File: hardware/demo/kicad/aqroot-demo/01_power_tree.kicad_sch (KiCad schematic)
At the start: 138 parts, among them J3 USB_C_Receptacle_USB2.0_16P, J4 BATTERY PIGTAIL 26AWG, Q2 NTMD4820N, Q3 NTMD4820N, Q4 BSS138, Q5 AO3401A, Q6 BSS138, Q7 BSS138, Q8 BSS138, Q9 BSS138, SW9 SW_SPDT, U10 USBLC6-2SC6, U11 BQ25185, U12 TPS63020, U13 TPS61023, U14 MAX17048, U18 LTC4368-1, U19 TLV7032, U20 TPS22950-Q1, U21 TPS61023, U22 TPS22950-Q1

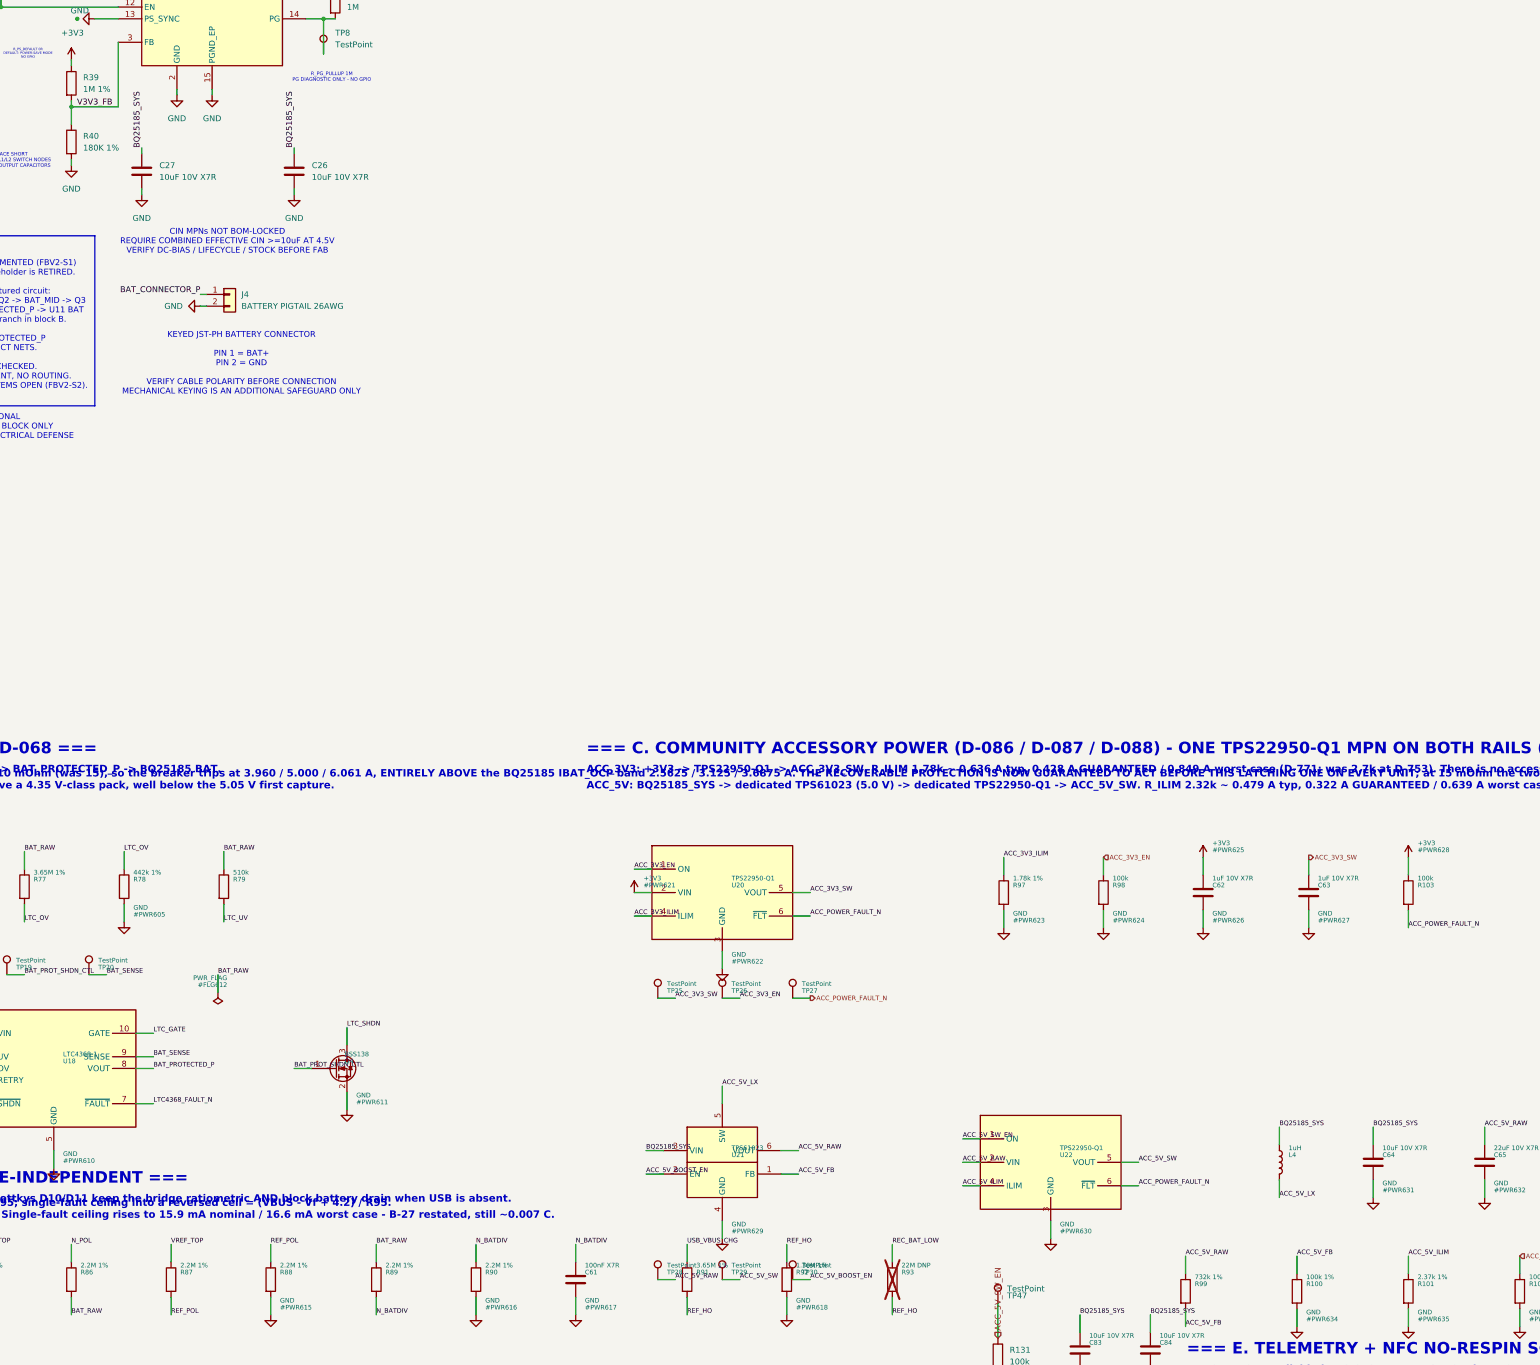
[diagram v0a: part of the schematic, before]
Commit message: demo: D-787 close Round-6 accessory-voltage contract and release proofs
R6-A01. The accessory proof costed +3V3 as an ideal 3.3 V source, so the
Community Port's published 3.135 V minimum was not guaranteed at the published
400 mA. F6 now derives the TPS63020 rail from the fitted divider, its value
tolerance, the SELECTED PART's TCR keyed to the purchased MPN, TI SLVS916I's
495/500/505 mV feedback band, 0.5% line and 0.5% load regulation, and the +5%
power-save high side.

R39 = 1 MOhm 0.1% / 25 ppm (Viking ARG03BTC1004) and R40 = 178 kOhm 0.1% /
25 ppm (Viking ARG03BTC1783). 176 kOhm was the first candidate and is refused
on AVAILABILITY: every 176 kOhm 0603 part at 0.1% or better in the JLCPCB
catalogue reads stock 0, including the KOA RN73H1JTTD1763B10 the first draft
locked, so it fails this repository's own rule_open_sourcing liquidity floor.
F7 now carries that as a clause -- every locked part must have an archived
exact-MPN live record clearing five boards x 10 -- with the zero-stock part and
a no-record part as refused controls.

Derived envelope: raw PWM 3.261337 / 3.308989 / 3.357013 V, heavy-load minimum
3.228806 V, power-save high 3.542487 V against the 3.600 V internal ceiling,
and 3.146366 V delivered at either J5 3.3 V contact at 400 mA against the
3.135 V contract, over the bounded U20->TP12 copper, the <=30 mOhm manual
first-five reinforcement lead and U20's 68 mOhm maximum RON. F6 proves off the
live netlist that TP12.1, J5.3 and J5.22 are all on /ACC_3V3_SW.

R101 = 2.43 kOhm guarantees 0.3065 A on ACC_5V and leaves the worst
user-reachable limiter state 1.49% below IBAT_OCP minimum. The dual loaded-VCELL
requirement re-derives to 3.8094 V -> 3.85 V firmware floor; single-rail is
3.1671 V so the 3.50 V policy stands.

R6-E01/E02. Both safety sequences move into a compiled host-tested seam and six
evasions are caught. New H8 proves the SHIPPED firmware calls that seam and
keeps no untested copy beside it. F5's three backlight controls, which an
ear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
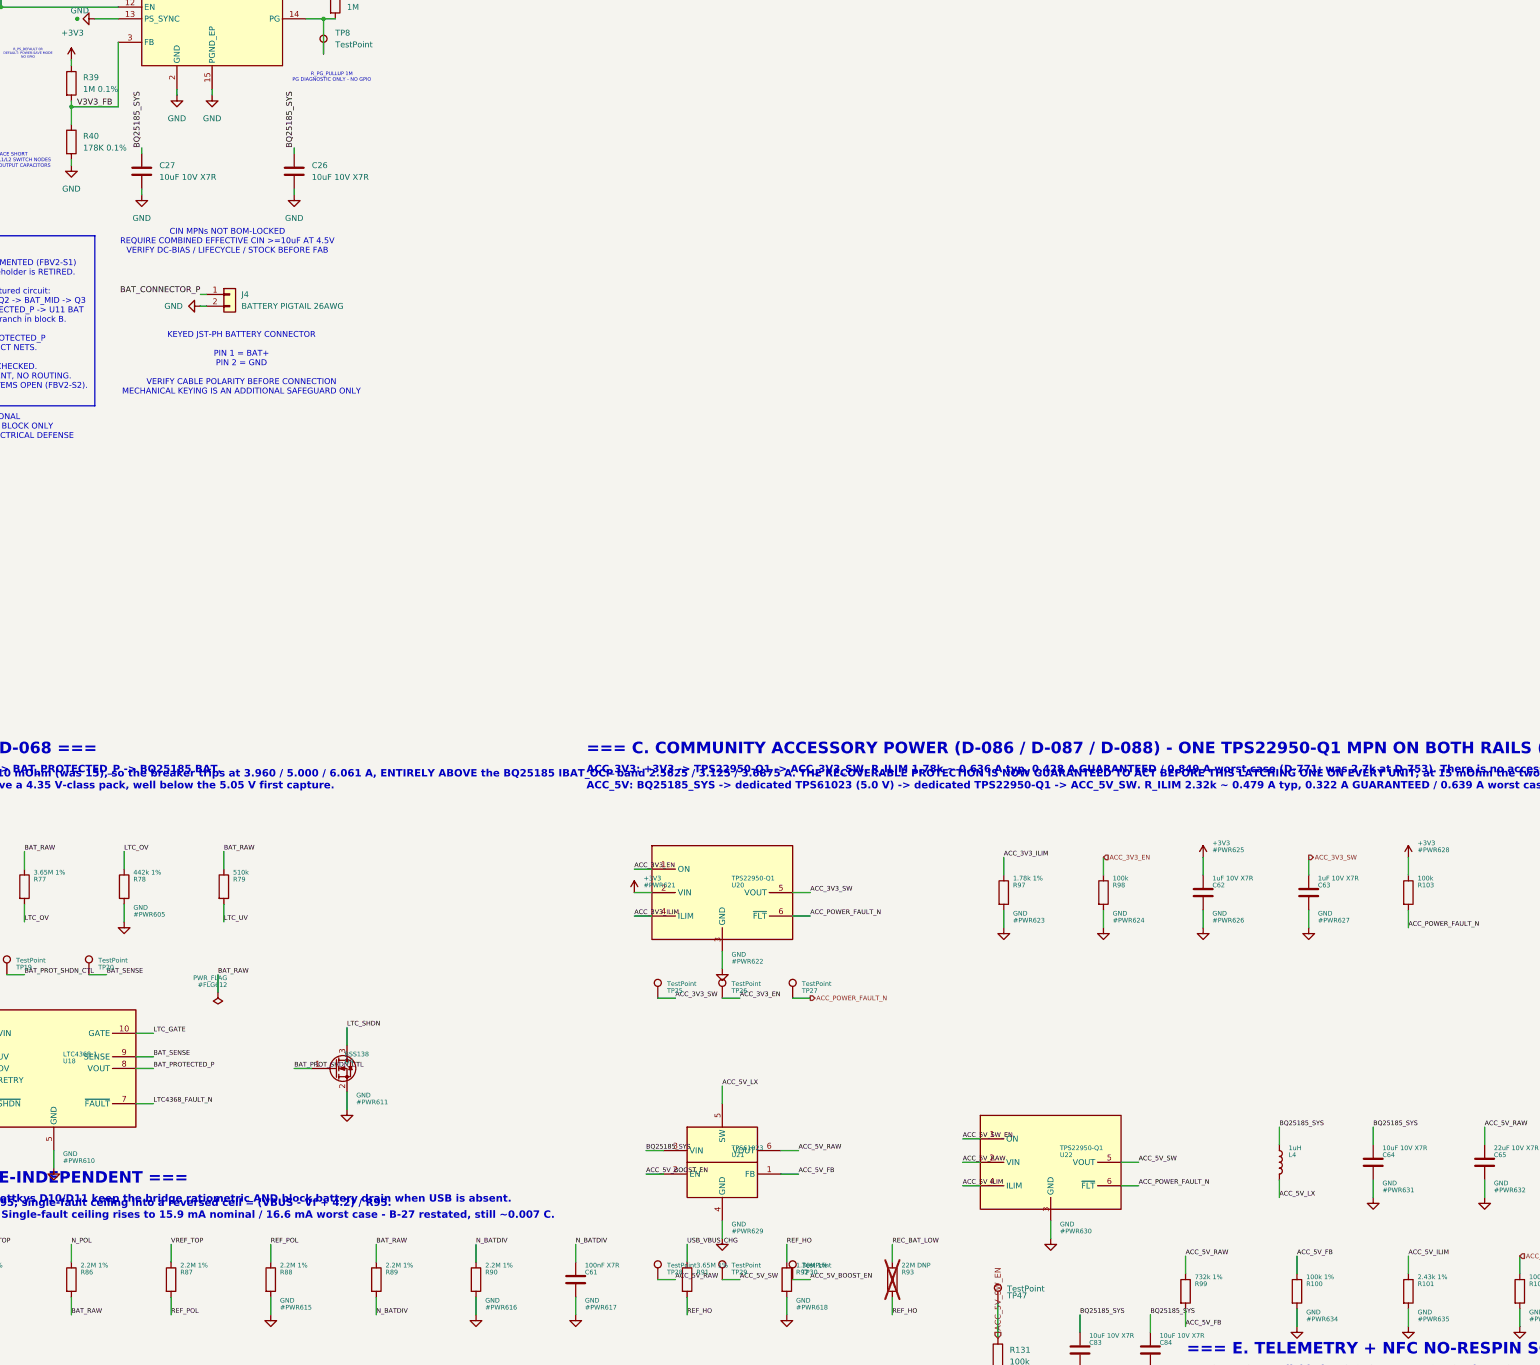
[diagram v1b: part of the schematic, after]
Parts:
- R101: value 2.37k 1% -> 2.43k 1%; LCSC C25964 -> C22906; MPN 0603WAF2371T5E -> 0603WAF2431T5E; Note D-773 THE 5 V SETPOINT WAS A NUMBER FROM A WRONG REFERENCE,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 -> D-787 / R6-A01 THE 5 V LIMITER SETTING MOVES AGAIN BECAUSE 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; Note_Sourcing SOURCING D-773 2026-09-19, verified live per D-096 through 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 -> SOURCING D-787 2026-09-20, verified live per D-096 through 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
- R39: value 1M 1% -> 1M 0.1%; LCSC C22935 -> C335092; MPN 0603WAF1004T5E -> ARG03BTC1004; Manufacturer UNI-ROYAL(Uniroyal Elec) -> Viking Tech; Note_Sourcing SOURCING D-614. EXACT_PRIOR from the beta-dm audit line '1M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 -> SOURCING D-787 2026-09-20, verified live per D-096 through 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
- R40: value 180K 1% -> 178K 0.1%; LCSC C22827 -> C2441185; MPN 0603WAF1803T5E -> ARG03BTC1783; Manufacturer UNI-ROYAL(Uniroyal Elec) -> Viking Tech; Note (none) -> D-787 / R6-A01 THE MAIN 3.3 V RAIL IS ADJUSTABLE AND ITS SE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; Note_Sourcing SOURCING D-614. EXACT_PRIOR from the beta-dm audit line '18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 -> SOURCING D-787 2026-09-20, verified live per D-096 through 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
